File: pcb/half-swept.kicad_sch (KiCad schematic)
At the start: 22 parts, among them J1 AudioJack4dpb, J2 AudioJack4dpb, SW1 SW_Push, SW10 SW_Push, SW11 SW_Push, SW12 SW_Push, SW14 SW_Push, SW15 SW_Push, SW16 SW_Push, SW17 SW_Push, SW18 SW_Push, SW2 SW_Push, SW20 SW_Push, SW21 SW_Push, SW3 SW_Push, SW4 SW_Push, SW5 SW_Push, SW6 SW_Push, SW8 SW_Push, SW9 SW_Push, U2 Elite-C

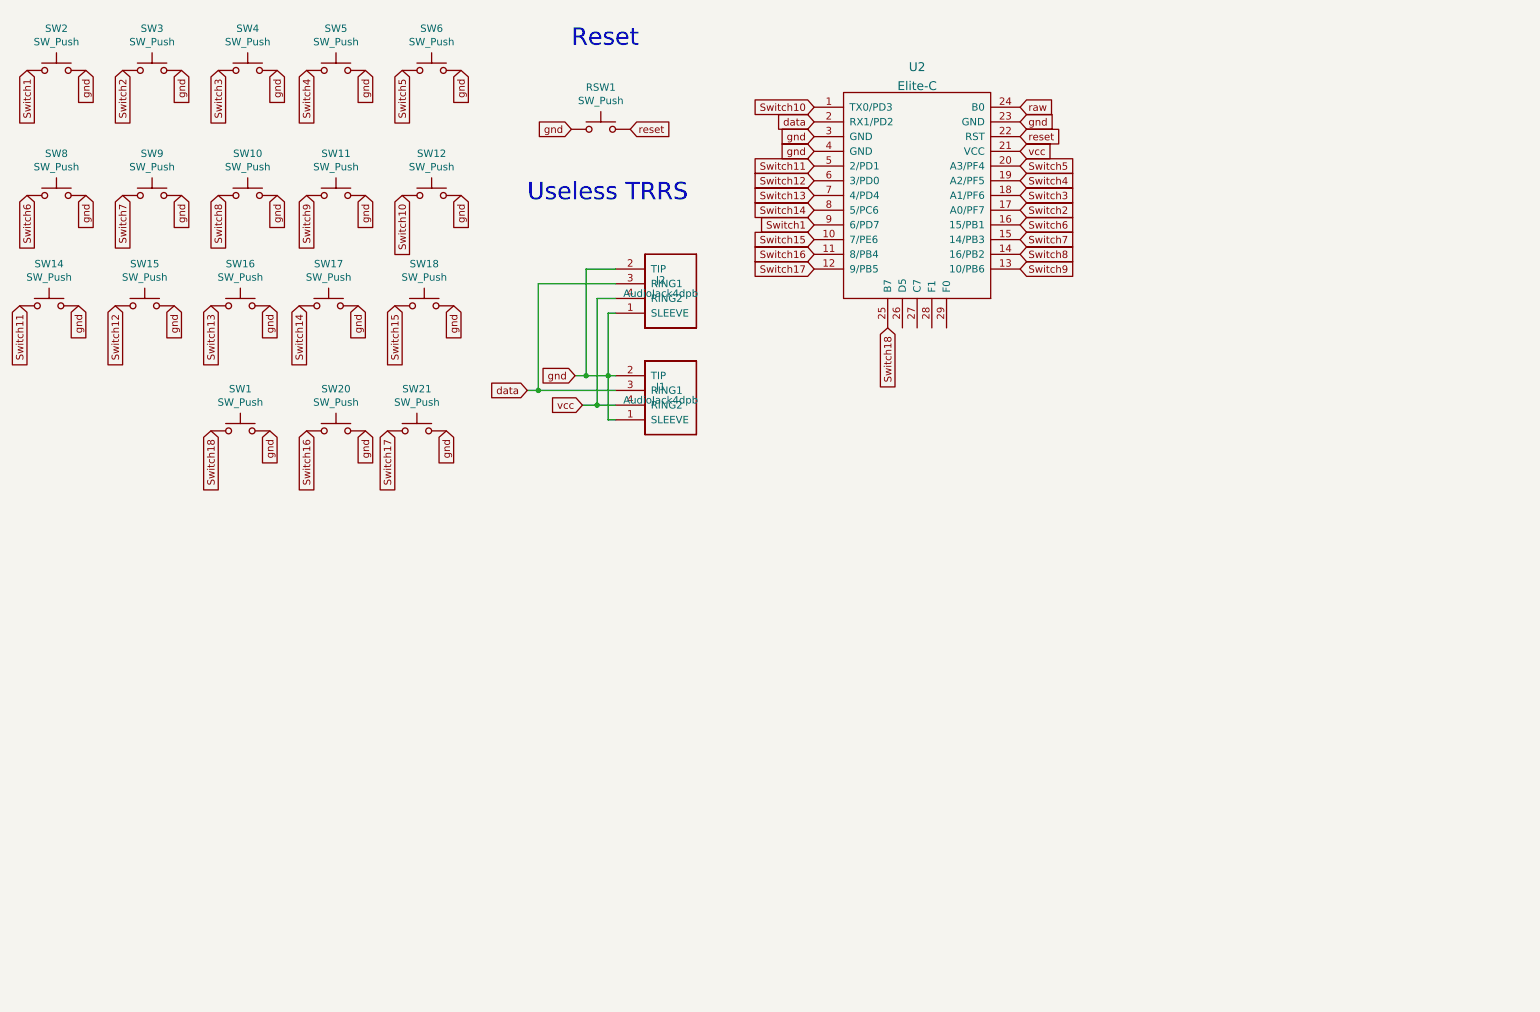
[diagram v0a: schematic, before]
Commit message: updated to include per key led support, oled support, 36 keys, still needs routing
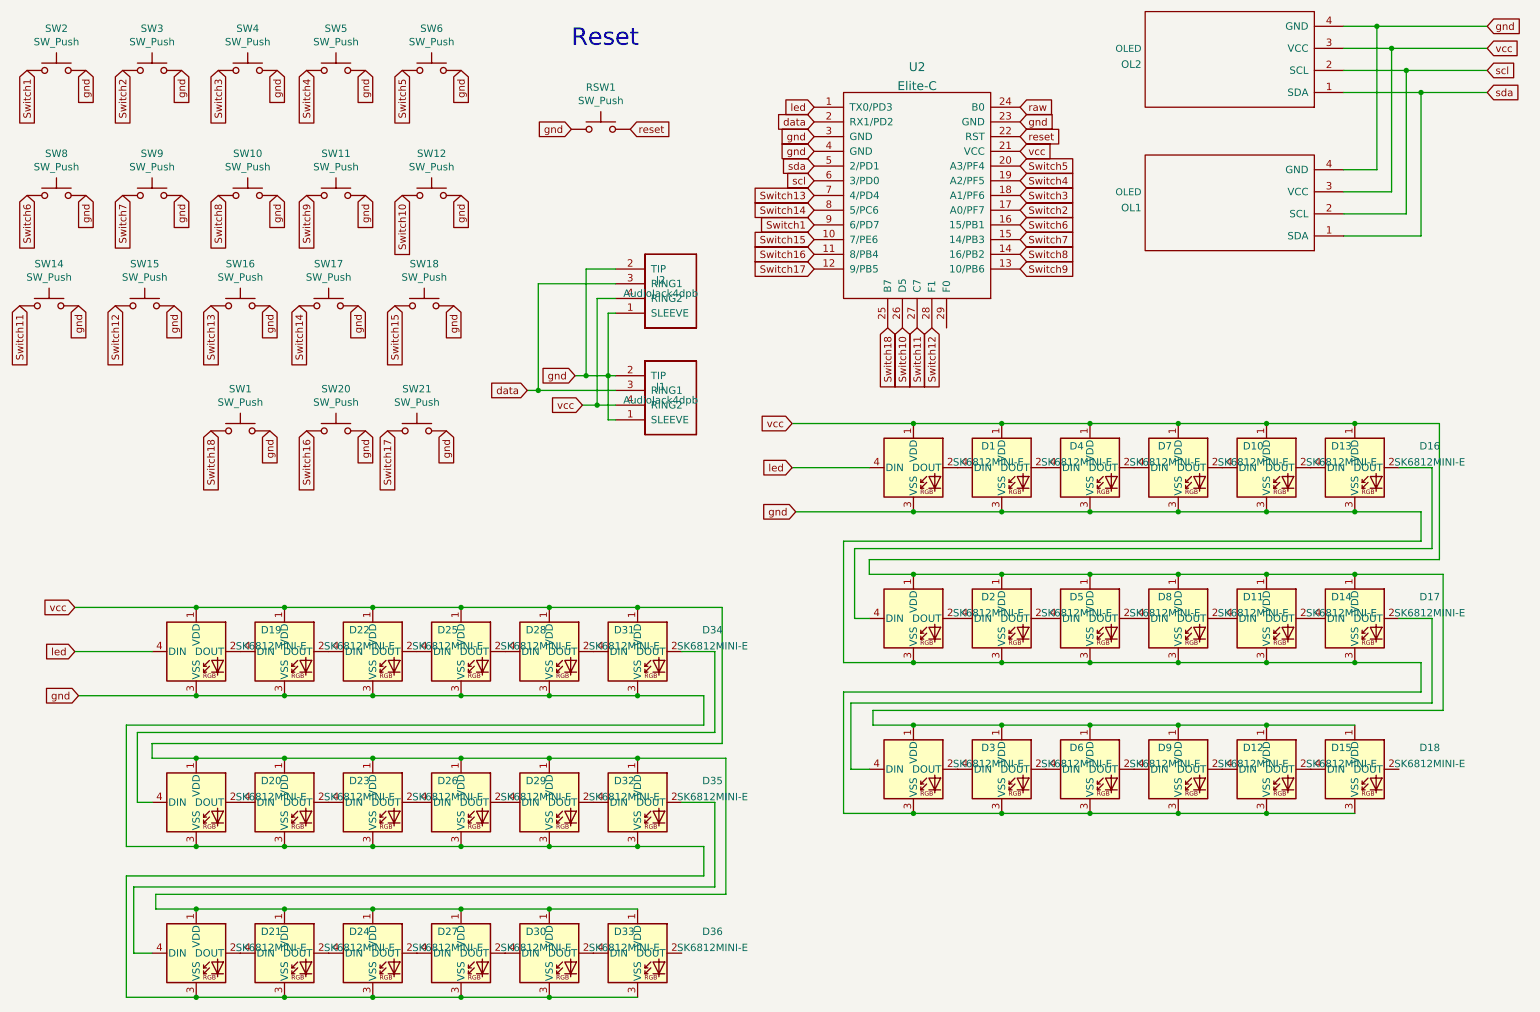
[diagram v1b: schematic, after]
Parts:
- added D1, D10, D11, D12, D13, D14, D15, D16, D17, D18, D19, D2, D20, D21, D22, D23, D24, D25, D26, D27, D28, D29, D3, D30, D31, D32, D33, D34, D35, D36, D4, D5, D6, D7, D8, D9: SK6812MINI-E, sweep36:MX_SK6812MINI-E_REV, symbol kicad-keyboard-parts:SK6812MINI-E
- added OL1, OL2: OLED, sweep36:OLED_v2, symbol kbd:OLED
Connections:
- net Switch10: now also U2.26 (D5); no longer U2.1 (TX0/PD3)
- net Switch11: now also U2.27 (C7); no longer U2.5 (2/PD1)
- net Switch12: now also U2.28 (F1); no longer U2.6 (3/PD0)
- net gnd: now also D1.3 (VSS), D10.3 (VSS), D11.3 (VSS), D12.3 (VSS), D13.3 (VSS), D14.3 (VSS), D15.3 (VSS), D16.3 (VSS), D17.3 (VSS), D18.3 (VSS), D19.3 (VSS), D2.3 (VSS), D20.3 (VSS), D21.3 (VSS), D22.3 (VSS), D23.3 (VSS), D24.3 (VSS), D25.3 (VSS), D26.3 (VSS), D27.3 (VSS), D28.3 (VSS), D29.3 (VSS), D3.3 (VSS), D30.3 (VSS), D31.3 (VSS), D32.3 (VSS), D33.3 (VSS), D34.3 (VSS), D35.3 (VSS), D36.3 (VSS), D4.3 (VSS), D5.3 (VSS), D6.3 (VSS), D7.3 (VSS), D8.3 (VSS), D9.3 (VSS), OL1.4 (GND), OL2.4 (GND)
- net vcc: now also D1.1 (VDD), D10.1 (VDD), D11.1 (VDD), D12.1 (VDD), D13.1 (VDD), D14.1 (VDD), D15.1 (VDD), D16.1 (VDD), D17.1 (VDD), D18.1 (VDD), D19.1 (VDD), D2.1 (VDD), D20.1 (VDD), D21.1 (VDD), D22.1 (VDD), D23.1 (VDD), D24.1 (VDD), D25.1 (VDD), D26.1 (VDD), D27.1 (VDD), D28.1 (VDD), D29.1 (VDD), D3.1 (VDD), D30.1 (VDD), D31.1 (VDD), D32.1 (VDD), D33.1 (VDD), D34.1 (VDD), D35.1 (VDD), D36.1 (VDD), D4.1 (VDD), D5.1 (VDD), D6.1 (VDD), D7.1 (VDD), D8.1 (VDD), D9.1 (VDD), OL1.3 (VCC), OL2.3 (VCC)
- new net: D20.4 (DIN), D34.2 (DOUT)
- new net: D31.2 (DOUT), D34.4 (DIN)
- new net: D25.2 (DOUT), D28.4 (DIN)
- new net: D22.2 (DOUT), D25.4 (DIN)
- new net: D14.2 (DOUT), D17.4 (DIN)
- new net: D11.2 (DOUT), D14.4 (DIN)
- new net: D17.2 (DOUT), D3.4 (DIN)
- new net: D20.2 (DOUT), D23.4 (DIN)
- new net: D6.2 (DOUT), D9.4 (DIN)
- new net: D3.2 (DOUT), D6.4 (DIN)
- new net: D32.2 (DOUT), D35.4 (DIN)
- new net: D29.2 (DOUT), D32.4 (DIN)
- new net: D12.2 (DOUT), D15.4 (DIN)
- new net: D12.4 (DIN), D9.2 (DOUT)
- new net: D33.2 (DOUT), D36.4 (DIN)
- new net: D15.2 (DOUT), D18.4 (DIN)
- new net: D28.2 (DOUT), D31.4 (DIN)
- new net: D26.2 (DOUT), D29.4 (DIN)
- new net: D23.2 (DOUT), D26.4 (DIN)
- new net: D11.4 (DIN), D8.2 (DOUT)
- new net: D5.2 (DOUT), D8.4 (DIN)
- new net: D1.2 (DOUT), D4.4 (DIN)
- new net: D2.2 (DOUT), D5.4 (DIN)
- new net: D16.2 (DOUT), D2.4 (DIN)
- new net: D24.2 (DOUT), D27.4 (DIN)
- new net: D21.2 (DOUT), D24.4 (DIN)
- new net: D19.2 (DOUT), D22.4 (DIN)
- new net: D10.2 (DOUT), D13.4 (DIN)
- new net: D10.4 (DIN), D7.2 (DOUT)
- new net: D4.2 (DOUT), D7.4 (DIN)
- new net: D30.2 (DOUT), D33.4 (DIN)
- new net: D27.2 (DOUT), D30.4 (DIN)
- new net: D13.2 (DOUT), D16.4 (DIN)
- new net: D21.4 (DIN), D35.2 (DOUT)
- new net led: D1.4 (DIN), D19.4 (DIN), U2.1 (TX0/PD3)
- new net scl: OL1.2 (SCL), OL2.2 (SCL), U2.6 (3/PD0)
- new net sda: OL1.1 (SDA), OL2.1 (SDA), U2.5 (2/PD1)
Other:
- note removed: "Useless TRRS"

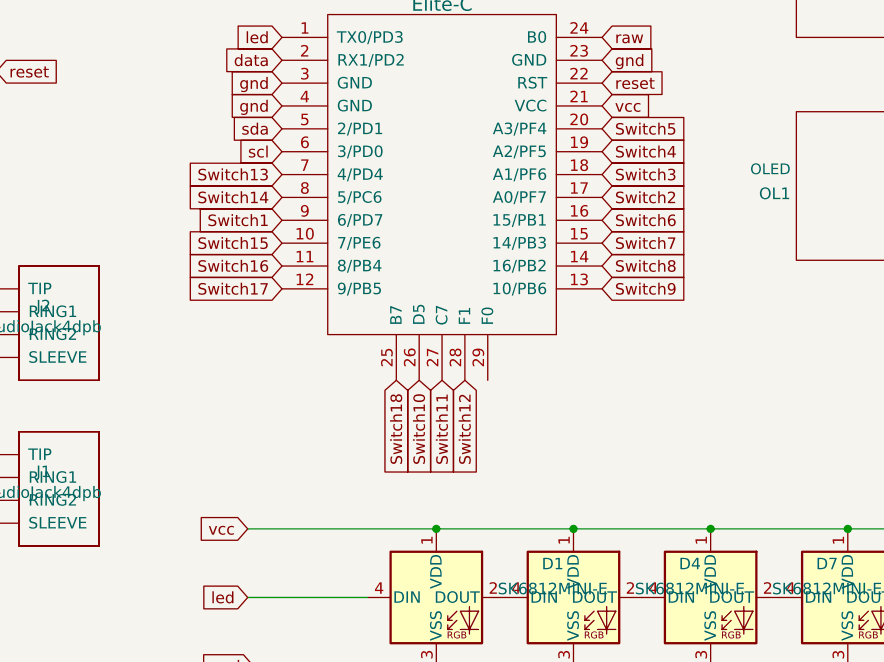
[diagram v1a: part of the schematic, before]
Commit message: finished routing to complete elite-c, oled, per key led, and 36 key support
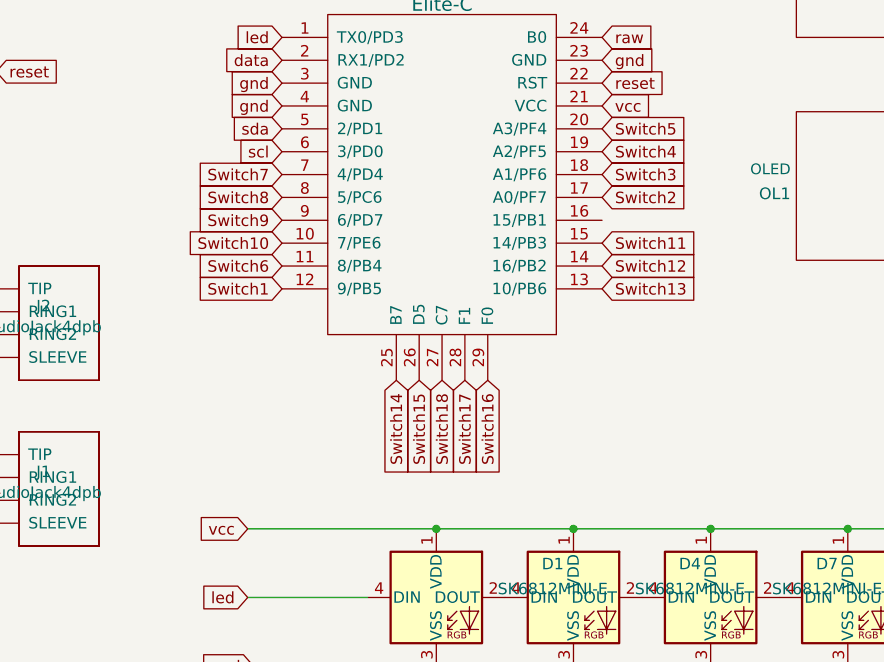
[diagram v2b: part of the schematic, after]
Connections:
- net Switch1: now also U2.12 (9/PB5); no longer U2.9 (6/PD7)
- net Switch10: now also U2.10 (7/PE6); no longer U2.26 (D5)
- net Switch11: now also U2.15 (14/PB3); no longer U2.27 (C7)
- net Switch12: now also U2.14 (16/PB2); no longer U2.28 (F1)
- net Switch13: now also U2.13 (10/PB6); no longer U2.7 (4/PD4)
- net Switch14: now also U2.25 (B7); no longer U2.8 (5/PC6)
- net Switch15: now also U2.26 (D5); no longer U2.10 (7/PE6)
- net Switch16: now also U2.29 (F0); no longer U2.11 (8/PB4)
- net Switch17: now also U2.28 (F1); no longer U2.12 (9/PB5)
- net Switch18: now also U2.27 (C7); no longer U2.25 (B7)
- net Switch6: now also U2.11 (8/PB4); no longer U2.16 (15/PB1)
- net Switch7: now also U2.7 (4/PD4); no longer U2.15 (14/PB3)
- net Switch8: now also U2.8 (5/PC6); no longer U2.14 (16/PB2)
- net Switch9: now also U2.9 (6/PD7); no longer U2.13 (10/PB6)
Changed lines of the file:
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@@
     )
   )
-  (global_label "Switch12" (shape input) (at 179.07 73.66 270) (fields_autoplaced)
-    (effects (font (size 1.27 1.27)) (justify right))
-    (property "Intersheet References" "${INTERSHEET_REFS}" (id 0) (at 130.81 232.41 0)
+  (global_label "Switch12" (shape input) (at 194.31 60.96 0) (fields_autoplaced)
+    (effects (font (size 1.27 1.27)) (justify left))
+    (property "Intersheet References" "${INTERSHEET_REFS}" (id 0) (at 353.06 109.22 0)
       (effects (font (size 1.27 1.27)) hide)
     )
@@
     )
   )
-  (global_label "Switch14" (shape input) (at 158.75 53.34 180) (fields_autoplaced)
-    (effects (font (size 1.27 1.27)) (justify right))
-    (property "Intersheet References" "${INTERSHEET_REFS}" (id 0) (at 0 0 0)
-      (effects (font (size 1.27 1.27)) hide)
-    )
-  )
-  (global_label "Switch13" (shape input) (at 158.75 50.8 180) (fields_autoplaced)
-    (effects (font (size 1.27 1.27)) (justify right))
-    (property "Intersheet References" "${INTERSHEET_REFS}" (id 0) (at 0 0 0)
+  (global_label "Switch14" (shape input) (at 171.45 73.66 270) (fields_autoplaced)
+    (effects (font (size 1.27 1.27)) (justify right))
+    (property "Intersheet References" "${INTERSHEET_REFS}" (id 0) (at 118.11 232.41 0)
+      (effects (font (size 1.27 1.27)) hide)
+    )
+  )
+  (global_label "Switch13" (shape input) (at 194.31 63.5 0) (fields_autoplaced)
+    (effects (font (size 1.27 1.27)) (justify left))
+    (property "Intersheet References" "${INTERSHEET_REFS}" (id 0) (at 353.06 114.3 0)
       (effects (font (size 1.27 1.27)) hide)
     )
@@
     )
   )
-  (global_label "Switch10" (shape input) (at 173.99 73.66 270) (fields_autoplaced)
-    (effects (font (size 1.27 1.27)) (justify right))
-    (property "Intersheet References" "${INTERSHEET_REFS}" (id 0) (at 138.43 232.41 0)
+  (global_label "Switch10" (shape input) (at 158.75 58.42 180) (fields_autoplaced)
+    (effects (font (size 1.27 1.27)) (justify right))
+    (property "Intersheet References" "${INTERSHEET_REFS}" (id 0) (at 0 22.86 0)
       (effects (font (size 1.27 1.27)) hide)
     )
@@
     )
   )
-  (global_label "Switch8" (shape input) (at 194.31 60.96 0) (fields_autoplaced)
-    (effects (font (size 1.27 1.27)) (justify left))
-    (property "Intersheet References" "${INTERSHEET_REFS}" (id 0) (at 0 0 0)
+  (global_label "Switch8" (shape input) (at 158.75 53.34 180) (fields_autoplaced)
+    (effects (font (size 1.27 1.27)) (justify right))
+    (property "Intersheet References" "${INTERSHEET_REFS}" (id 0) (at 353.06 114.3 0)
       (effects (font (size 1.27 1.27)) hide)
     )
@@
     )
   )
-  (global_label "Switch7" (shape input) (at 194.31 58.42 0) (fields_autoplaced)
-    (effects (font (size 1.27 1.27)) (justify left))
-    (property "Intersheet References" "${INTERSHEET_REFS}" (id 0) (at 0 0 0)
+  (global_label "Switch7" (shape input) (at 158.75 50.8 180) (fields_autoplaced)
+    (effects (font (size 1.27 1.27)) (justify right))
+    (property "Intersheet References" "${INTERSHEET_REFS}" (id 0) (at 353.06 109.22 0)
       (effects (font (size 1.27 1.27)) hide)
     )
@@
     )
   )
-  (global_label "Switch1" (shape input) (at 158.75 55.88 180) (fields_autoplaced)
-    (effects (font (size 1.27 1.27)) (justify right))
-    (property "Intersheet References" "${INTERSHEET_REFS}" (id 0) (at 0 0 0)
+  (global_label "Switch1" (shape input) (at 158.75 63.5 180) (fields_autoplaced)
+    (effects (font (size 1.27 1.27)) (justify right))
+    (property "Intersheet References" "${INTERSHEET_REFS}" (id 0) (at 0 7.62 0)
       (effects (font (size 1.27 1.27)) hide)
     )
@@
     )
   )
-  (global_label "Switch9" (shape input) (at 194.31 63.5 0) (fields_autoplaced)
-    (effects (font (size 1.27 1.27)) (justify left))
-    (property "Intersheet References" "${INTERSHEET_REFS}" (id 0) (at 0 0 0)
+  (global_label "Switch9" (shape input) (at 158.75 55.88 180) (fields_autoplaced)
+    (effects (font (size 1.27 1.27)) (justify right))
+    (property "Intersheet References" "${INTERSHEET_REFS}" (id 0) (at 353.06 119.38 0)
       (effects (font (size 1.27 1.27)) hide)
     )
@@
     )
   )
-  (global_label "Switch6" (shape input) (at 194.31 55.88 0) (fields_autoplaced)
-    (effects (font (size 1.27 1.27)) (justify left))
-    (property "Intersheet References" "${INTERSHEET_REFS}" (id 0) (at 0 0 0)
+  (global_label "Switch6" (shape input) (at 158.75 60.96 180) (fields_autoplaced)
+    (effects (font (size 1.27 1.27)) (justify right))
+    (property "Intersheet References" "${INTERSHEET_REFS}" (id 0) (at 353.06 116.84 0)
       (effects (font (size 1.27 1.27)) hide)
     )
@@
     )
   )
-  (global_label "Switch16" (shape input) (at 158.75 60.96 180) (fields_autoplaced)
-    (effects (font (size 1.27 1.27)) (justify right))
-    (property "Intersheet References" "${INTERSHEET_REFS}" (id 0) (at 0 0 0)
+  (global_label "Switch16" (shape input) (at 181.61 73.66 270) (fields_autoplaced)
+    (effects (font (size 1.27 1.27)) (justify right))
+    (property "Intersheet References" "${INTERSHEET_REFS}" (id 0) (at 120.65 232.41 0)
       (effects (font (size 1.27 1.27)) hide)
     )
@@
     )
   )
-  (global_label "Switch15" (shape input) (at 158.75 58.42 180) (fields_autoplaced)
-    (effects (font (size 1.27 1.27)) (justify right))
-    (property "Intersheet References" "${INTERSHEET_REFS}" (id 0) (at 0 0 0)
+  (global_label "Switch15" (shape input) (at 173.99 73.66 270) (fields_autoplaced)
+    (effects (font (size 1.27 1.27)) (justify right))
+    (property "Intersheet References" "${INTERSHEET_REFS}" (id 0) (at 115.57 232.41 0)
       (effects (font (size 1.27 1.27)) hide)
     )
@@
     )
   )
-  (global_label "Switch17" (shape input) (at 158.75 63.5 180) (fields_autoplaced)
-    (effects (font (size 1.27 1.27)) (justify right))
-    (property "Intersheet References" "${INTERSHEET_REFS}" (id 0) (at 0 0 0)
+  (global_label "Switch17" (shape input) (at 179.07 73.66 270) (fields_autoplaced)
+    (effects (font (size 1.27 1.27)) (justify right))
+    (property "Intersheet References" "${INTERSHEET_REFS}" (id 0) (at 115.57 232.41 0)
       (effects (font (size 1.27 1.27)) hide)
     )
@@
     )
   )
-  (global_label "Switch11" (shape input) (at 176.53 73.66 270) (fields_autoplaced)
-    (effects (font (size 1.27 1.27)) (justify right))
-    (property "Intersheet References" "${INTERSHEET_REFS}" (id 0) (at 130.81 232.41 0)
+  (global_label "Switch11" (shape input) (at 194.31 58.42 0) (fields_autoplaced)
+    (effects (font (size 1.27 1.27)) (justify left))
+    (property "Intersheet References" "${INTERSHEET_REFS}" (id 0) (at 353.06 104.14 0)
       (effects (font (size 1.27 1.27)) hide)
     )
@@
     )
   )
-  (global_label "Switch18" (shape input) (at 171.45 73.66 270) (fields_autoplaced)
-    (effects (font (size 1.27 1.27)) (justify right))
-    (property "Intersheet References" "${INTERSHEET_REFS}" (id 0) (at 171.3706 84.5113 90)
-      (effects (font (size 1.27 1.27)) (justify right) hide)
-    )
+  (global_label "Switch18" (shape input) (at 176.53 73.66 270) (fields_autoplaced)
+    (effects (font (size 1.27 1.27)) (justify right))
+    (property "Intersheet References" "${INTERSHEET_REFS}" (id 0) (at 176.4506 84.5113 90)
+      (effects (font (size 1.27 1.27)) (justify right) hide)
+    )

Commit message: added gateron ks-27 support on the same footprint, so now supports both choc v1 and ks-27
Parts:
- SW1, SW10, SW11, SW12, SW14, SW15, SW16, SW17, SW18, SW2, SW20, SW21, SW3, SW4, SW5, SW6, SW8, SW9: footprint Keebio-Parts:Kailh-PG1350-1u-reversible -> fingerpunch:gateron-ks27-choc-v1-reversible
